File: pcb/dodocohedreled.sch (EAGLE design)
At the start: 11 parts

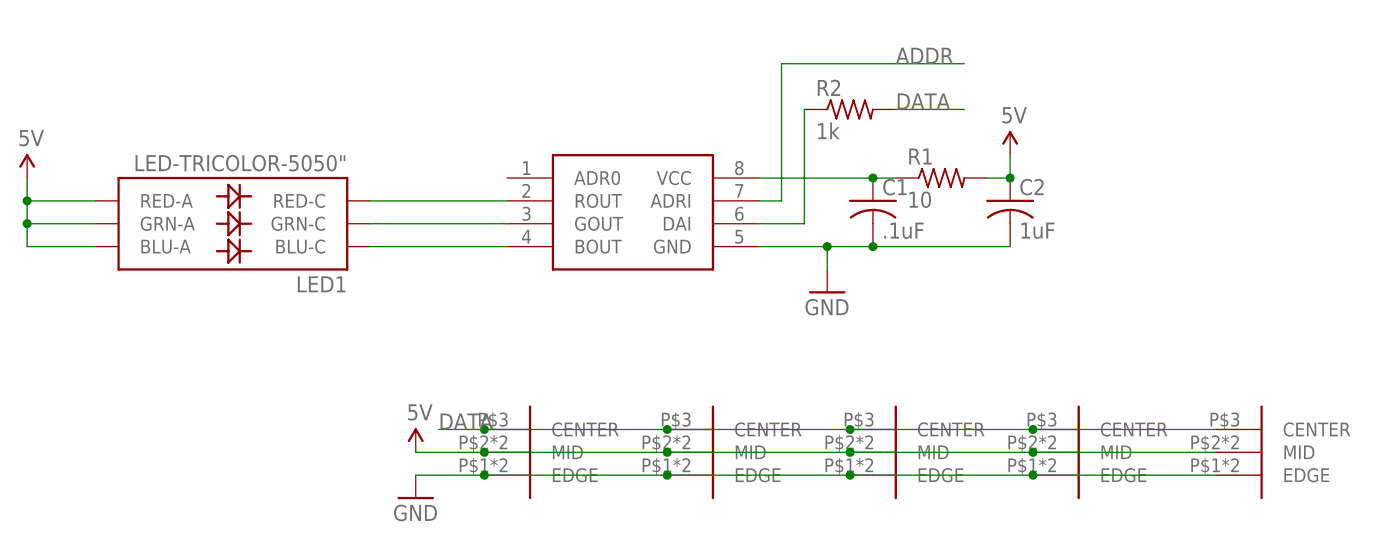
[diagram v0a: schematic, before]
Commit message: Move all components to top side
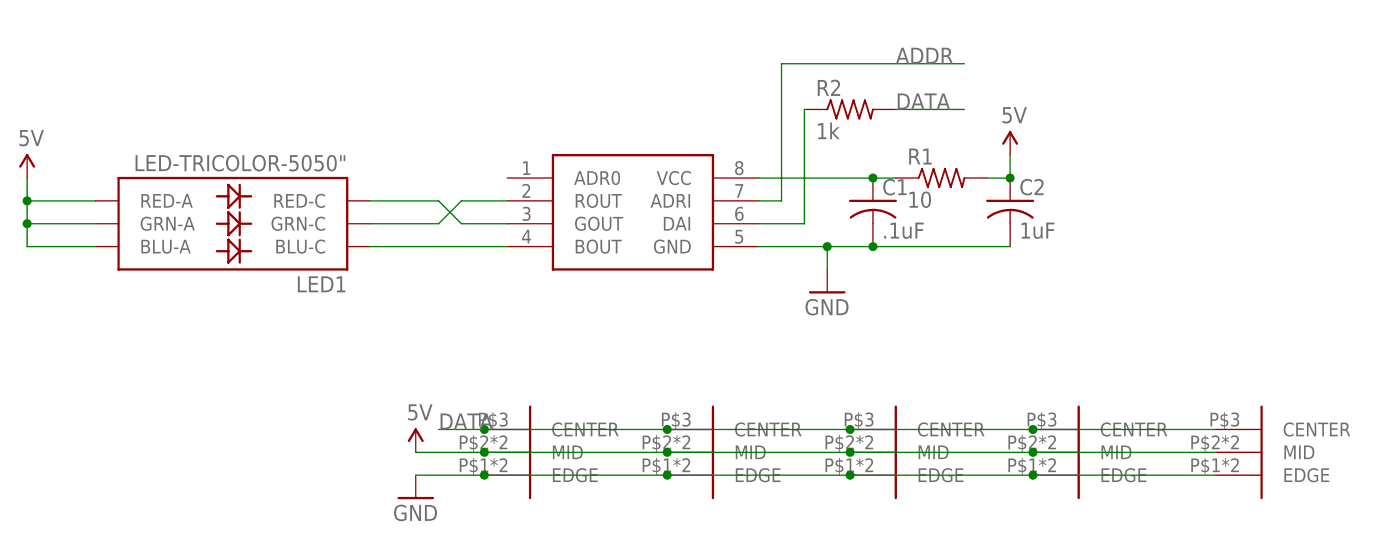
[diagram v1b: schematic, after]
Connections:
- removed net N$4: LED1.RED-C, U$1.ROUT
- new net N$1: LED1.GRN-C, U$1.ROUT
- net N$3: now also LED1.RED-C; no longer LED1.GRN-C
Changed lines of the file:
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@@
-</segment>
-</net>
-<net name="N$3" class="0">
-<segment>
-<pinref part="U$1" gate="G$1" pin="GOUT"/>
-<pinref part="LED1" gate="G$1" pin="GRN-C"/>
-<wire x1="45.72" y1="81.28" x2="30.48" y2="81.28" width="0.1524" layer="91"/>
-</segment>
-</net>
-<net name="N$4" class="0">
-<segment>
-<pinref part="LED1" gate="G$1" pin="RED-C"/>
-<pinref part="U$1" gate="G$1" pin="ROUT"/>
-<wire x1="30.48" y1="83.82" x2="45.72" y2="83.82" width="0.1524" layer="91"/>
 </segment>
 </net>
@@
 </segment>
 </net>
+<net name="N$1" class="0">
+<segment>
+<pinref part="U$1" gate="G$1" pin="ROUT"/>
+<wire x1="45.72" y1="83.82" x2="40.64" y2="83.82" width="0.1524" layer="91"/>
+<wire x1="40.64" y1="83.82" x2="38.1" y2="81.28" width="0.1524" layer="91"/>
+<pinref part="LED1" gate="G$1" pin="GRN-C"/>
+<wire x1="38.1" y1="81.28" x2="30.48" y2="81.28" width="0.1524" layer="91"/>
+</segment>
+</net>
+<net name="N$3" class="0">
+<segment>
+<pinref part="LED1" gate="G$1" pin="RED-C"/>
+<wire x1="30.48" y1="83.82" x2="38.1" y2="83.82" width="0.1524" layer="91"/>
+<wire x1="38.1" y1="83.82" x2="40.64" y2="81.28" width="0.1524" layer="91"/>
+<pinref part="U$1" gate="G$1" pin="GOUT"/>
+<wire x1="40.64" y1="81.28" x2="45.72" y2="81.28" width="0.1524" layer="91"/>
+</segment>
+</net>

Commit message: Update for RevC
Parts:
- U$2, U$3, U$4, U$5, U$6: value D_EDGE -> D_EDGESLOT; device dodocohedreled:D_EDGE -> dodocohedreled:D_EDGESLOT
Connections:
- net 5V: now also U$2.5V, U$3.5V, U$4.5V, U$5.5V, U$6.5V; no longer U$2.MID, U$3.MID, U$4.MID, U$5.MID, U$6.MID
- net DATA: now also U$2.DATA, U$3.DATA, U$4.DATA, U$5.DATA, U$6.DATA; no longer U$2.CENTER, U$3.CENTER, U$4.CENTER, U$5.CENTER, U$6.CENTER
- net GND: now also U$2.GND, U$3.GND, U$4.GND, U$5.GND, U$6.GND; no longer U$2.EDGE, U$3.EDGE, U$4.EDGE, U$5.EDGE, U$6.EDGE
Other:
- moved on the sheet: C1, C2, R1
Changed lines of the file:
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@@
 <part name="R2" library="adafruit" deviceset="R-US_" device="R0603" value="1k"/>
 <part name="SUPPLY2" library="SparkFun-Aesthetics" deviceset="5V" device=""/>
-<part name="U$2" library="dodocohedreled" deviceset="D_EDGE" device=""/>
+<part name="U$2" library="dodocohedreled" deviceset="D_EDGE" device="SLOT"/>
 <part name="SUPPLY3" library="SparkFun-Aesthetics" deviceset="5V" device=""/>
 <part name="GND2" library="SparkFun-Aesthetics" deviceset="GND" device=""/>
-<part name="U$3" library="dodocohedreled" deviceset="D_EDGE" device=""/>
-<part name="U$4" library="dodocohedreled" deviceset="D_EDGE" device=""/>
-<part name="U$5" library="dodocohedreled" deviceset="D_EDGE" device=""/>
-<part name="U$6" library="dodocohedreled" deviceset="D_EDGE" device=""/>
+<part name="U$3" library="dodocohedreled" deviceset="D_EDGE" device="SLOT"/>
+<part name="U$4" library="dodocohedreled" deviceset="D_EDGE" device="SLOT"/>
+<part name="U$5" library="dodocohedreled" deviceset="D_EDGE" device="SLOT"/>
+<part name="U$6" library="dodocohedreled" deviceset="D_EDGE" device="SLOT"/>
 </parts>
 <sheets>
@@
 <instance part="GND1" gate="1" x="81.28" y="73.66"/>
 <instance part="U$1" gate="G$1" x="53.34" y="81.28"/>
-<instance part="C1" gate="G$1" x="86.36" y="83.82"/>
-<instance part="C2" gate="G$1" x="101.6" y="83.82"/>
-<instance part="R1" gate="G$1" x="93.98" y="86.36"/>
+<instance part="C1" gate="G$1" x="104.14" y="83.82"/>
+<instance part="C2" gate="G$1" x="119.38" y="83.82"/>
+<instance part="R1" gate="G$1" x="111.76" y="86.36"/>
 <instance part="R2" gate="G$1" x="83.82" y="93.98"/>
-<instance part="SUPPLY2" gate="G$1" x="101.6" y="88.9"/>
+<instance part="SUPPLY2" gate="G$1" x="119.38" y="88.9"/>
 <instance part="U$2" gate="G$1" x="124.46" y="58.42"/>
 <instance part="SUPPLY3" gate="G$1" x="35.56" y="55.88"/>
@@
 <pinref part="R1" gate="G$1" pin="2"/>
 <pinref part="C2" gate="G$1" pin="1"/>
-<wire x1="99.06" y1="86.36" x2="101.6" y2="86.36" width="0.1524" layer="91"/>
+<wire x1="116.84" y1="86.36" x2="119.38" y2="86.36" width="0.1524" layer="91"/>
 <pinref part="SUPPLY2" gate="G$1" pin="5V"/>
-<wire x1="101.6" y1="88.9" x2="101.6" y2="86.36" width="0.1524" layer="91"/>
-<junction x="101.6" y="86.36"/>
+<wire x1="119.38" y1="88.9" x2="119.38" y2="86.36" width="0.1524" layer="91"/>
+<junction x="119.38" y="86.36"/>
 </segment>
 <segment>
-<pinref part="U$2" gate="G$1" pin="MID"/>
+<pinref part="U$2" gate="G$1" pin="5V"/>
 <wire x1="124.46" y1="55.88" x2="104.14" y2="55.88" width="0.1524" layer="91"/>
 <pinref part="SUPPLY3" gate="G$1" pin="5V"/>
-<pinref part="U$3" gate="G$1" pin="MID"/>
+<pinref part="U$3" gate="G$1" pin="5V"/>
 <wire x1="104.14" y1="55.88" x2="83.82" y2="55.88" width="0.1524" layer="91"/>
 <wire x1="83.82" y1="55.88" x2="63.5" y2="55.88" width="0.1524" layer="91"/>
 <wire x1="63.5" y1="55.88" x2="43.18" y2="55.88" width="0.1524" layer="91"/>
 <junction x="63.5" y="55.88"/>
-<pinref part="U$4" gate="G$1" pin="MID"/>
+<pinref part="U$4" gate="G$1" pin="5V"/>
 <wire x1="43.18" y1="55.88" x2="35.56" y2="55.88" width="0.1524" layer="91"/>
 <junction x="43.18" y="55.88"/>
-<pinref part="U$5" gate="G$1" pin="MID"/>
+<pinref part="U$5" gate="G$1" pin="5V"/>
 <junction x="83.82" y="55.88"/>
-<pinref part="U$6" gate="G$1" pin="MID"/>
+<pinref part="U$6" gate="G$1" pin="5V"/>
 <junction x="104.14" y="55.88"/>
 </segment>
@@
 <pinref part="C2" gate="G$1" pin="2"/>
 <pinref part="C1" gate="G$1" pin="2"/>
-<wire x1="101.6" y1="78.74" x2="86.36" y2="78.74" width="0.1524" layer="91"/>
-<wire x1="86.36" y1="78.74" x2="81.28" y2="78.74" width="0.1524" layer="91"/>
+<wire x1="119.38" y1="78.74" x2="104.14" y2="78.74" width="0.1524" layer="91"/>
+<wire x1="104.14" y1="78.74" x2="81.28" y2="78.74" width="0.1524" layer="91"/>
 <junction x="81.28" y="78.74"/>
-<junction x="86.36" y="78.74"/>
+<junction x="104.14" y="78.74"/>
 </segment>
 <segment>
-<pinref part="U$2" gate="G$1" pin="EDGE"/>
+<pinref part="U$2" gate="G$1" pin="GND"/>
 <wire x1="124.46" y1="53.34" x2="104.14" y2="53.34" width="0.1524" layer="91"/>
 <pinref part="GND2" gate="1" pin="GND"/>
-<pinref part="U$3" gate="G$1" pin="EDGE"/>
+<pinref part="U$3" gate="G$1" pin="GND"/>
 <wire x1="104.14" y1="53.34" x2="83.82" y2="53.34" width="0.1524" layer="91"/>
 <wire x1="83.82" y1="53.34" x2="63.5" y2="53.34" width="0.1524" layer="91"/>
 <wire x1="63.5" y1="53.34" x2="43.18" y2="53.34" width="0.1524" layer="91"/>
 <junction x="63.5" y="53.34"/>
-<pinref part="U$4" gate="G$1" pin="EDGE"/>
+<pinref part="U$4" gate="G$1" pin="GND"/>
 <wire x1="43.18" y1="53.34" x2="35.56" y2="53.34" width="0.1524" layer="91"/>
 <junction x="43.18" y="53.34"/>
-<pinref part="U$5" gate="G$1" pin="EDGE"/>
+<pinref part="U$5" gate="G$1" pin="GND"/>
 <junction x="83.82" y="53.34"/>
-<pinref part="U$6" gate="G$1" pin="EDGE"/>
+<pinref part="U$6" gate="G$1" pin="GND"/>
 <junction x="104.14" y="53.34"/>
 </segment>
@@
 <pinref part="U$1" gate="G$1" pin="VCC"/>
 <pinref part="C1" gate="G$1" pin="1"/>
-<wire x1="73.66" y1="86.36" x2="86.36" y2="86.36" width="0.1524" layer="91"/>
+<wire x1="73.66" y1="86.36" x2="73.66" y2="104.14" width="0.1524" layer="91"/>
+<wire x1="73.66" y1="104.14" x2="104.14" y2="104.14" width="0.1524" layer="91"/>
+<wire x1="104.14" y1="104.14" x2="104.14" y2="86.36" width="0.1524" layer="91"/>
 <pinref part="R1" gate="G$1" pin="1"/>
-<wire x1="86.36" y1="86.36" x2="88.9" y2="86.36" width="0.1524" layer="91"/>
-<junction x="86.36" y="86.36"/>
+<wire x1="104.14" y1="86.36" x2="106.68" y2="86.36" width="0.1524" layer="91"/>
+<junction x="104.14" y="86.36"/>
 </segment>
 </net>
@@
 </segment>
 <segment>
-<pinref part="U$2" gate="G$1" pin="CENTER"/>
+<pinref part="U$2" gate="G$1" pin="DATA"/>
 <wire x1="124.46" y1="58.42" x2="104.14" y2="58.42" width="0.1524" layer="91"/>
 <label x="38.1" y="58.42" size="1.778" layer="95"/>
-<pinref part="U$3" gate="G$1" pin="CENTER"/>
+<pinref part="U$3" gate="G$1" pin="DATA"/>
 <wire x1="104.14" y1="58.42" x2="83.82" y2="58.42" width="0.1524" layer="91"/>
 <wire x1="83.82" y1="58.42" x2="63.5" y2="58.42" width="0.1524" layer="91"/>
 <wire x1="63.5" y1="58.42" x2="43.18" y2="58.42" width="0.1524" layer="91"/>
 <junction x="63.5" y="58.42"/>
-<pinref part="U$4" gate="G$1" pin="CENTER"/>
+<pinref part="U$4" gate="G$1" pin="DATA"/>
 <wire x1="43.18" y1="58.42" x2="38.1" y2="58.42" width="0.1524" layer="91"/>
 <junction x="43.18" y="58.42"/>
-<pinref part="U$5" gate="G$1" pin="CENTER"/>
+<pinref part="U$5" gate="G$1" pin="DATA"/>
 <junction x="83.82" y="58.42"/>
-<pinref part="U$6" gate="G$1" pin="CENTER"/>
+<pinref part="U$6" gate="G$1" pin="DATA"/>
 <junction x="104.14" y="58.42"/>
 </segment>
